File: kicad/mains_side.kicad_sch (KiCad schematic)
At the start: 39 parts, among them P1 Conn_WallPlug, Q1 Q_Photo_NPN, U2 B179

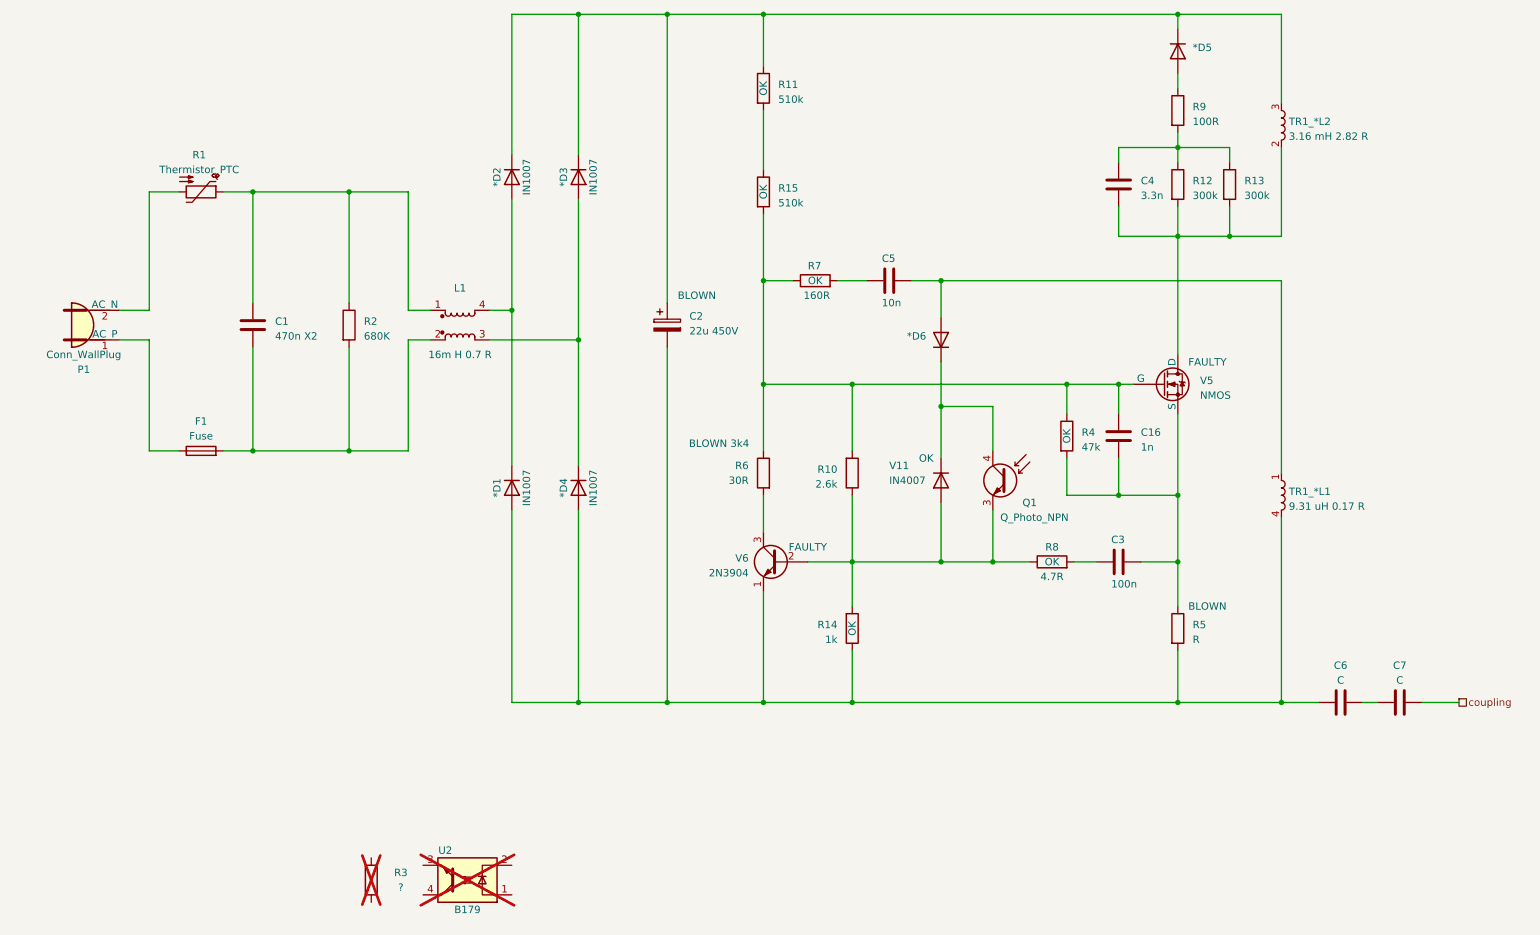
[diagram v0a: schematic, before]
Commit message: Add footprints
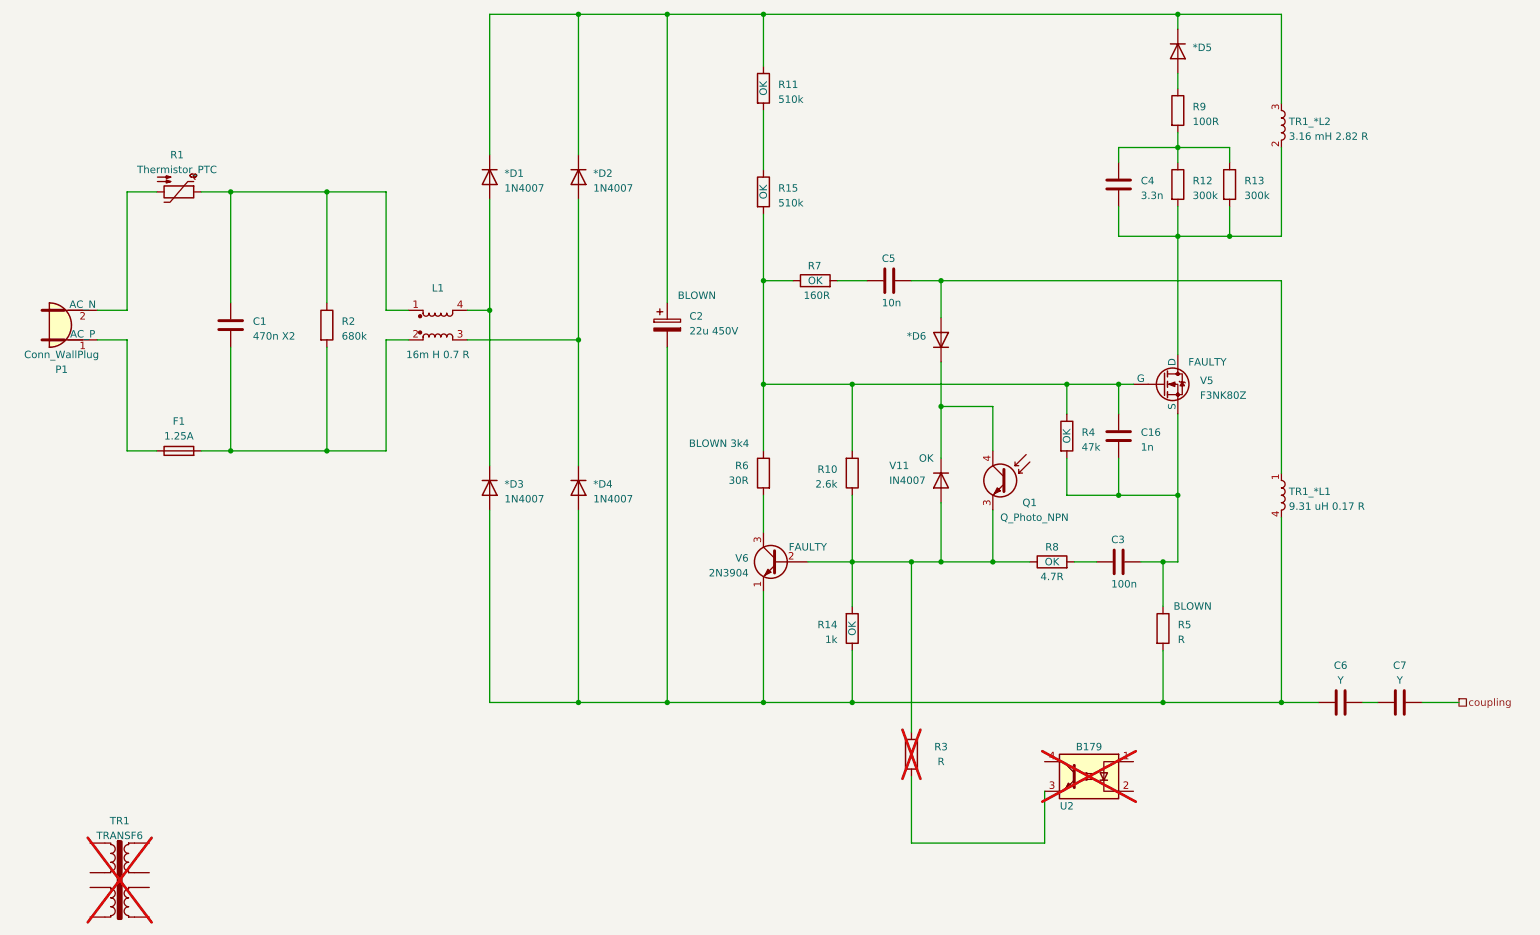
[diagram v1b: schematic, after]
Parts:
- removed *D1, *D2, *D3, *D4: IN1007, symbol Device:D
- added *D1, *D2, *D3, *D4: 1N4007, Diode_THT:D_DO-41_SOD81_P10.16mm_Horizontal, symbol Diode:1N4007
- added TR1: TRANSF6, symbol Transformer:TRANSF6
- *D5, *D6: footprint (none) -> Diode_THT:D_DO-41_SOD81_P10.16mm_Horizontal
- C6, C7: value C -> Y
- F1: value Fuse -> 1.25A; footprint (none) -> Fuse:Fuse_SunFuse-6HP; Speed (none) -> Slow; Voltage (none) -> 350 VAC / 120 VC
- Q1: now left out of the parts list
- R1, R10, R11, R12, R13, R14, R15, R4, R5, R6, R7, R8, R9: footprint (none) -> Resistor_THT:R_Axial_DIN0207_L6.3mm_D2.5mm_P10.16mm_Horizontal
- R2: value 680K -> 680k; footprint (none) -> Resistor_THT:R_Axial_DIN0207_L6.3mm_D2.5mm_P10.16mm_Horizontal
- R3: value ? -> R; footprint (none) -> Resistor_THT:R_Axial_DIN0207_L6.3mm_D2.5mm_P10.16mm_Horizontal
- V5: value NMOS -> F3NK80Z; footprint (none) -> Package_TO_SOT_THT:TO-220-3_Vertical
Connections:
- net at C2.2, C6.1, R14.1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: now also *D3.2 (A), *D4.2 (A)
- net at Q1.3 (E), R10.1, R14.2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: now also R3.2
- net at U2.3: now also R3.1
- net at L1.3: now also *D2.2 (A), *D4.1 (K)
- net at L1.4: now also *D1.2 (A), *D3.1 (K)
- net at *D5.1 (K), C2.1, R11.1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: now also *D1.1 (K), *D2.1 (K)
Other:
- moved on the sheet: C1, F1, L1, P1, R1, R2, R3, R5, U2

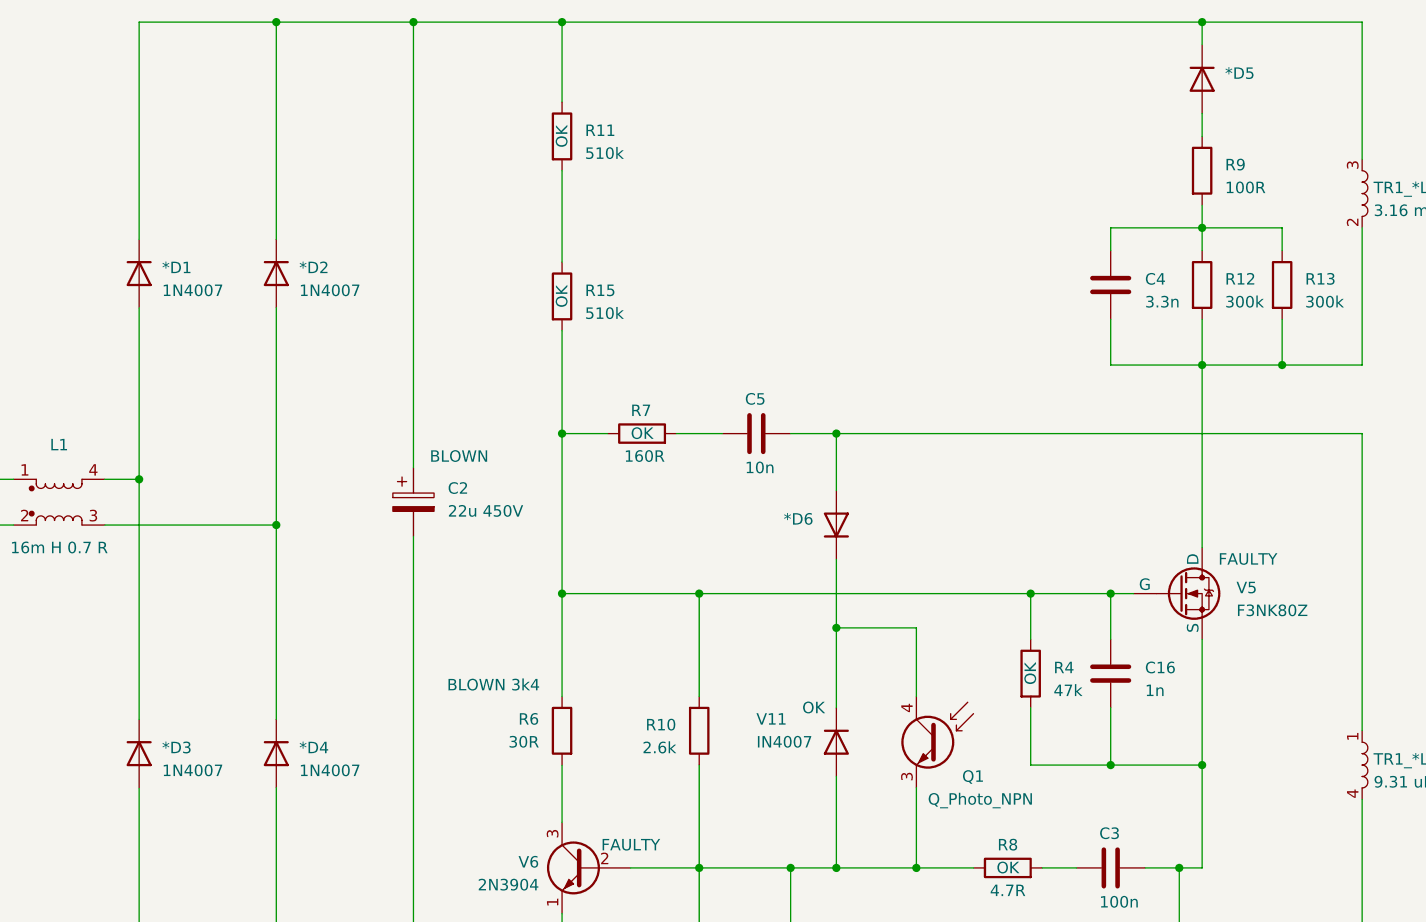
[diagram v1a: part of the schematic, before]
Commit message: Fix symbol names
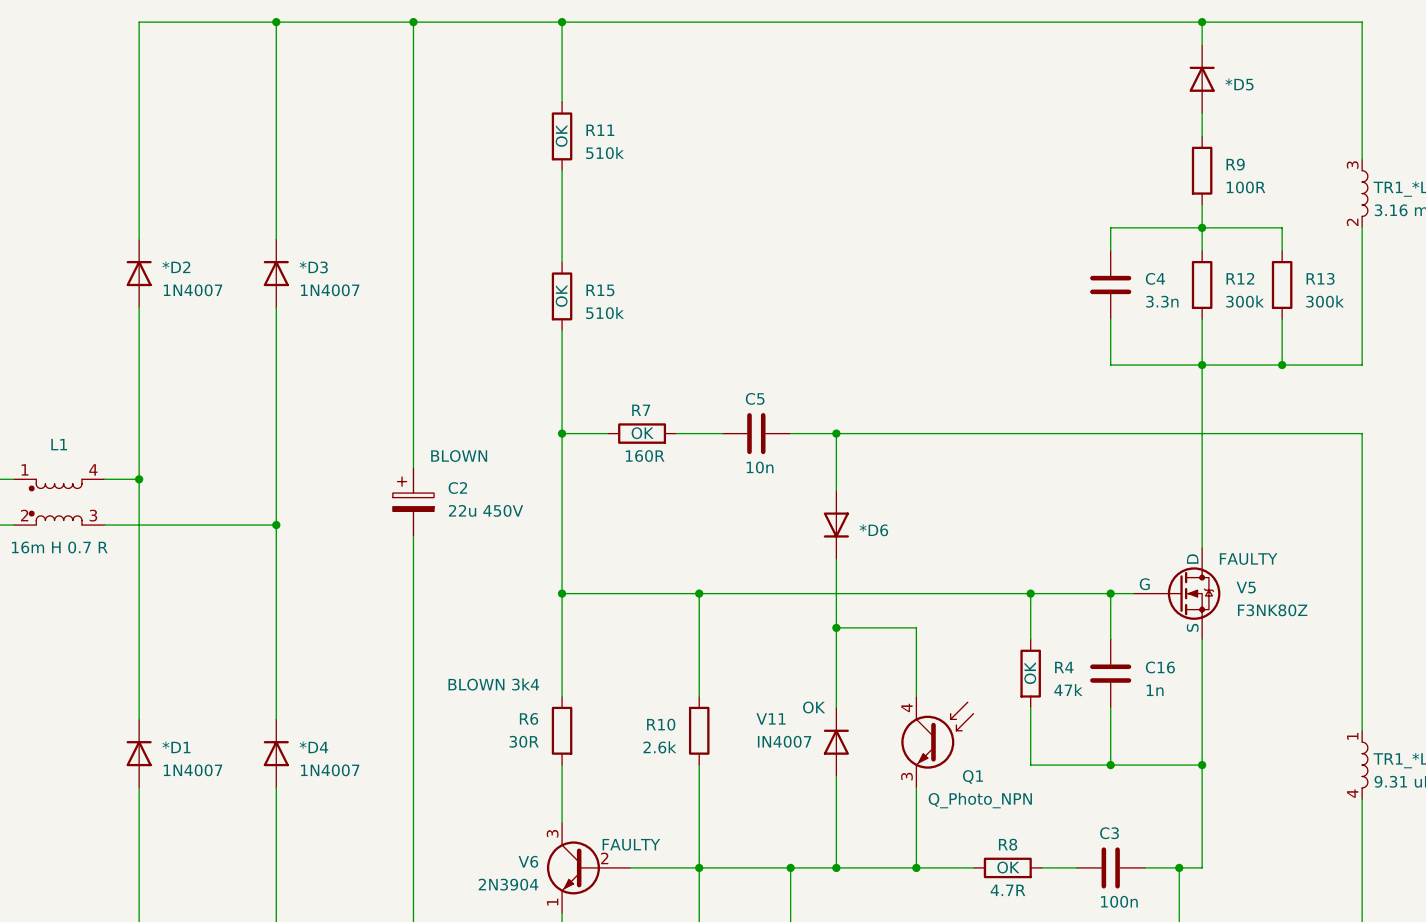
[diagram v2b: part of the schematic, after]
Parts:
- renumbered *D3 to *D1, *D1 to *D2, *D2 to *D3
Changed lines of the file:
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@@
         )
         (path "/ab18b4c8-6f40-44db-bccd-b69c22b3ada9/4c8f6a8b-06f4-4e61-8fed-29a27b18ce1c"
-          (reference "R9") (unit 1)
+          (reference "R14") (unit 1)
         )
       )
@@
         )
         (path "/ab18b4c8-6f40-44db-bccd-b69c22b3ada9/4c8f6a8b-06f4-4e61-8fed-29a27b18ce1c"
-          (reference "R19") (unit 1)
+          (reference "R13") (unit 1)
         )
       )
@@
         )
         (path "/ab18b4c8-6f40-44db-bccd-b69c22b3ada9/4c8f6a8b-06f4-4e61-8fed-29a27b18ce1c"
-          (reference "TR1_*L2") (unit 1)
+          (reference "TR1_*L1") (unit 1)
         )
       )
@@
         )
         (path "/ab18b4c8-6f40-44db-bccd-b69c22b3ada9/4c8f6a8b-06f4-4e61-8fed-29a27b18ce1c"
-          (reference "R13") (unit 1)
+          (reference "R9") (unit 1)
         )
       )
@@
         )
         (path "/ab18b4c8-6f40-44db-bccd-b69c22b3ada9/4c8f6a8b-06f4-4e61-8fed-29a27b18ce1c"
-          (reference "C5") (unit 1)
+          (reference "C16") (unit 1)
         )
       )
@@
         )
         (path "/ab18b4c8-6f40-44db-bccd-b69c22b3ada9/4c8f6a8b-06f4-4e61-8fed-29a27b18ce1c"
-          (reference "V2") (unit 1)
+          (reference "V11") (unit 1)
         )
       )
@@
         )
         (path "/ab18b4c8-6f40-44db-bccd-b69c22b3ada9/4c8f6a8b-06f4-4e61-8fed-29a27b18ce1c"
-          (reference "R8") (unit 1)
+          (reference "R10") (unit 1)
         )
       )
@@
   (symbol (lib_id "Diode:1N4007") (at 101.6 113.03 270) (unit 1)
     (in_bom yes) (on_board yes) (dnp no) (fields_autoplaced)
-    (property "Reference" "*D3" (at 104.14 112.395 90)
+    (property "Reference" "*D1" (at 104.14 112.395 90)
       (effects (font (size 1.27 1.27)) (justify left))
     )
@@
       (project "Dremel_PCB1857_V1"
         (path "/ab18b4c8-6f40-44db-bccd-b69c22b3ada9/4c8f6a8b-06f4-4e61-8fed-29a27b18ce1c"
-          (reference "*D3") (unit 1)
+          (reference "*D1") (unit 1)
         )
       )
@@
   (symbol (lib_id "Diode:1N4007") (at 101.6 59.69 270) (unit 1)
     (in_bom yes) (on_board yes) (dnp no) (fields_autoplaced)
-    (property "Reference" "*D1" (at 104.14 59.055 90)
+    (property "Reference" "*D2" (at 104.14 59.055 90)
       (effects (font (size 1.27 1.27)) (justify left))
     )
@@
       (project "Dremel_PCB1857_V1"
         (path "/ab18b4c8-6f40-44db-bccd-b69c22b3ada9/4c8f6a8b-06f4-4e61-8fed-29a27b18ce1c"
-          (reference "*D1") (unit 1)
+          (reference "*D2") (unit 1)
         )
       )
@@
         )
         (path "/ab18b4c8-6f40-44db-bccd-b69c22b3ada9/4c8f6a8b-06f4-4e61-8fed-29a27b18ce1c"
-          (reference "R11") (unit 1)
+          (reference "R4") (unit 1)
         )
       )
@@
   (symbol (lib_id "Diode:1N4007") (at 116.84 59.69 270) (unit 1)
     (in_bom yes) (on_board yes) (dnp no) (fields_autoplaced)
-    (property "Reference" "*D2" (at 119.38 59.055 90)
+    (property "Reference" "*D3" (at 119.38 59.055 90)
       (effects (font (size 1.27 1.27)) (justify left))
     )
@@
       (project "Dremel_PCB1857_V1"
         (path "/ab18b4c8-6f40-44db-bccd-b69c22b3ada9/4c8f6a8b-06f4-4e61-8fed-29a27b18ce1c"
-          (reference "*D2") (unit 1)
+          (reference "*D3") (unit 1)
         )
       )
@@
         )
         (path "/ab18b4c8-6f40-44db-bccd-b69c22b3ada9/4c8f6a8b-06f4-4e61-8fed-29a27b18ce1c"
-          (reference "R10") (unit 1)
+          (reference "R8") (unit 1)
         )
       )
@@
         )
         (path "/ab18b4c8-6f40-44db-bccd-b69c22b3ada9/4c8f6a8b-06f4-4e61-8fed-29a27b18ce1c"
-          (reference "C7") (unit 1)
+          (reference "C6") (unit 1)
         )
       )
@@
   (symbol (lib_id "Device:D") (at 179.07 87.63 270) (mirror x) (unit 1)
     (in_bom yes) (on_board yes) (dnp no) (fields_autoplaced)
-    (property "Reference" "*D6" (at 176.53 86.995 90)
-      (effects (font (size 1.27 1.27)) (justify right))
+    (property "Reference" "*D6" (at 181.61 88.265 90)
+      (effects (font (size 1.27 1.27)) (justify left))
     )
     (property "Value" "D" (at 176.53 89.535 90)
@@
         )
         (path "/ab18b4c8-6f40-44db-bccd-b69c22b3ada9/4c8f6a8b-06f4-4e61-8fed-29a27b18ce1c"
-          (reference "*D5") (unit 1)
+          (reference "*D6") (unit 1)
         )
       )
@@
         )
         (path "/ab18b4c8-6f40-44db-bccd-b69c22b3ada9/4c8f6a8b-06f4-4e61-8fed-29a27b18ce1c"
-          (reference "V3") (unit 1)
+          (reference "V5") (unit 1)
         )
       )
@@
         )
         (path "/ab18b4c8-6f40-44db-bccd-b69c22b3ada9/4c8f6a8b-06f4-4e61-8fed-29a27b18ce1c"
-          (reference "C3") (unit 1)
+          (reference "C5") (unit 1)
         )
       )
@@
         )
         (path "/ab18b4c8-6f40-44db-bccd-b69c22b3ada9/4c8f6a8b-06f4-4e61-8fed-29a27b18ce1c"
-          (reference "R14") (unit 1)
+          (reference "R12") (unit 1)
         )
       )
@@
         )
         (path "/ab18b4c8-6f40-44db-bccd-b69c22b3ada9/4c8f6a8b-06f4-4e61-8fed-29a27b18ce1c"
-          (reference "TR1_*L1") (unit 1)
+          (reference "TR1_*L2") (unit 1)
         )
       )
@@
         )
         (path "/ab18b4c8-6f40-44db-bccd-b69c22b3ada9/4c8f6a8b-06f4-4e61-8fed-29a27b18ce1c"
-          (reference "C6") (unit 1)
+          (reference "C3") (unit 1)
         )
       )
@@
         )
         (path "/ab18b4c8-6f40-44db-bccd-b69c22b3ada9/4c8f6a8b-06f4-4e61-8fed-29a27b18ce1c"
-          (reference "C10") (unit 1)
+          (reference "C7") (unit 1)
         )
       )
@@
         )
         (path "/ab18b4c8-6f40-44db-bccd-b69c22b3ada9/4c8f6a8b-06f4-4e61-8fed-29a27b18ce1c"
-          (reference "R5") (unit 1)
+          (reference "R15") (unit 1)
         )
       )
@@
         )
         (path "/ab18b4c8-6f40-44db-bccd-b69c22b3ada9/4c8f6a8b-06f4-4e61-8fed-29a27b18ce1c"
-          (reference "R4") (unit 1)
+          (reference "R11") (unit 1)
         )
       )
@@
   (symbol (lib_id "Device:D") (at 219.71 38.1 270) (unit 1)
     (in_bom yes) (on_board yes) (dnp no) (fields_autoplaced)
-    (property "Reference" "*D5" (at 222.25 37.465 90)
+    (property "Reference" "*D5" (at 222.25 38.735 90)
       (effects (font (size 1.27 1.27)) (justify left))
     )
@@
         )
         (path "/ab18b4c8-6f40-44db-bccd-b69c22b3ada9/4c8f6a8b-06f4-4e61-8fed-29a27b18ce1c"
-          (reference "*D6") (unit 1)
-        )
-      )
+          (reference "*D5") (unit 1)
+        )
+      )

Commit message: Update schematic
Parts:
- removed U2: B179, Package_DIP:DIP-4_W7.62mm, symbol Isolator:EL817
- added Q1: Q_Photo_NPN, symbol Device:Q_Photo_NPN
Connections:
- net at Q1.3 (E), R10.1, R14.2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: now also R3.1; no longer R3.2
- net at C16.1, R15.2, R4.1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: no longer R10.2
- net at *D6.1 (K), Q1.4 (C), V11.1 (K): now also R10.2, Q1.4 (C)
- new net: Q1.3 (E), R3.2
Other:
- moved on the sheet: *D5, *D6, C16, C3, C4, C5, C6, C7, Q1, R10, R12, R13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
